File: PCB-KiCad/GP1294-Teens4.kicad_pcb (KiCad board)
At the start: 2 copper layers, 178.3 x 100.1 mm, 51 parts, among them IC1 74132D, IC2 XL6009, IC3 ZXBM5210, SW1 SW_DPDT_x2, SW2 SW_DPDT_x2, SW3 SW_DPDT_x2, SW4 SW_DPDT_x2, SW5 SW_DPDT_x2, U3 R-78B5.0-2.0, U5 ATtiny84A-P, U6 74HC165, U7 74HC165, U8 CS8421

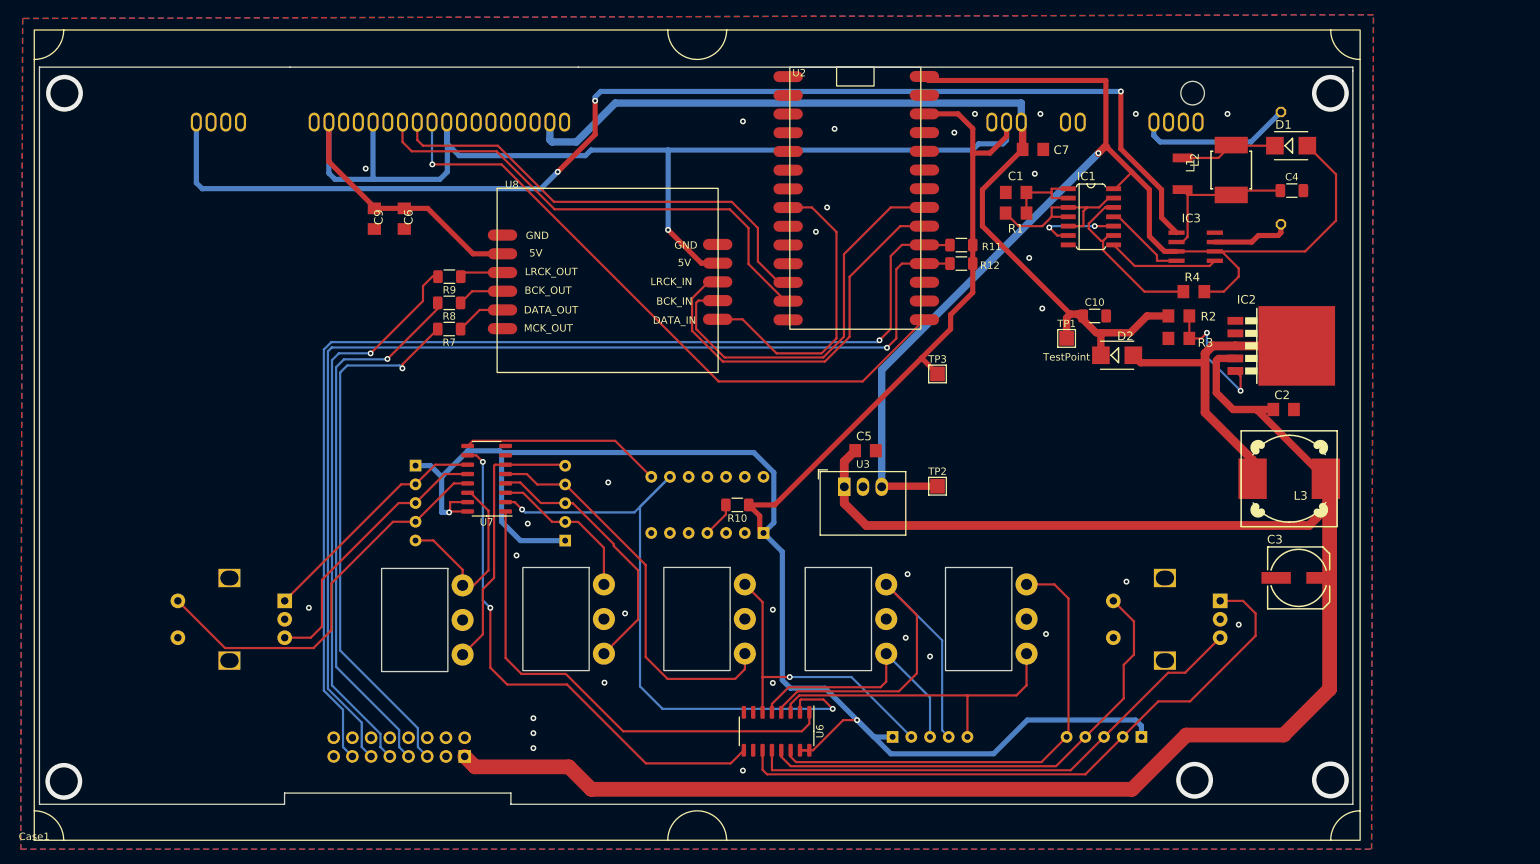
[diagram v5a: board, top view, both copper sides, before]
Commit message: Added OLED 5.5" option
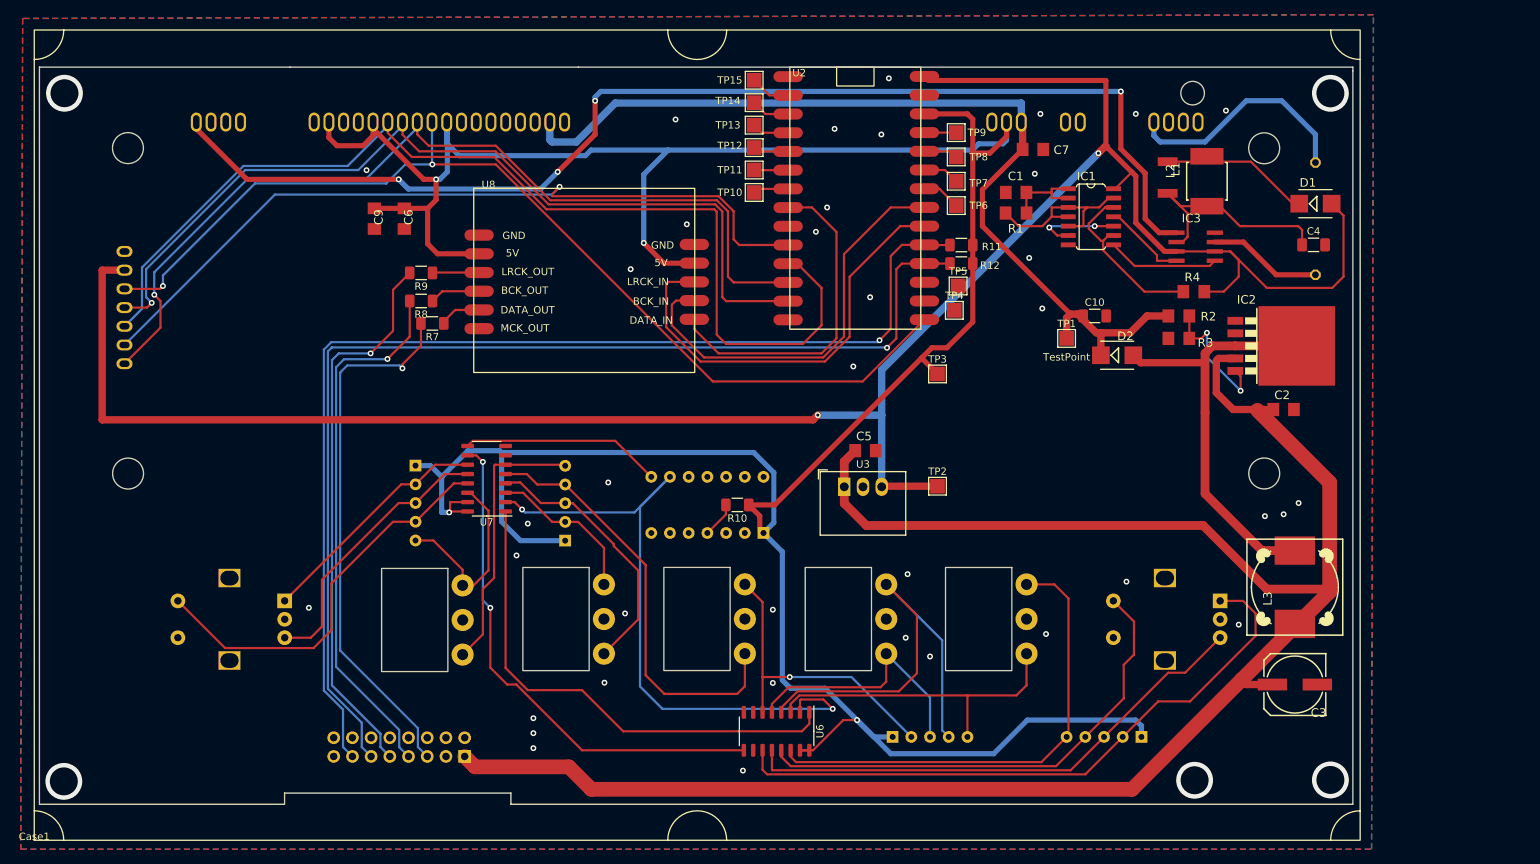
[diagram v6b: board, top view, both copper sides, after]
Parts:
- added TP10: TestPoint, TestPoint:TestPoint_Pad_2.0x2.0mm, F.Cu at (157.7, 67.1)
- added TP11: TestPoint, TestPoint:TestPoint_Pad_2.0x2.0mm, F.Cu at (157.7, 64.0)
- added TP12: TestPoint, TestPoint:TestPoint_Pad_2.0x2.0mm, F.Cu at (157.7, 61.0)
- added TP13: TestPoint, TestPoint:TestPoint_Pad_2.0x2.0mm, F.Cu at (157.7, 57.9)
- added TP14: TestPoint, TestPoint:TestPoint_Pad_2.0x2.0mm, F.Cu at (157.7, 54.9)
- added TP15: TestPoint, TestPoint:TestPoint_Pad_2.0x2.0mm, F.Cu at (157.7, 51.8)
- added TP4: TestPoint, TestPoint:TestPoint_Pad_2.0x2.0mm, F.Cu at (184.9, 83.1)
- added TP5: TestPoint, TestPoint:TestPoint_Pad_2.0x2.0mm, F.Cu at (185.4, 79.8)
- added TP6: TestPoint, TestPoint:TestPoint_Pad_2.0x2.0mm, F.Cu at (185.2, 68.8)
- added TP7: TestPoint, TestPoint:TestPoint_Pad_2.0x2.0mm, F.Cu at (185.2, 65.5)
- added TP8: TestPoint, TestPoint:TestPoint_Pad_2.0x2.0mm, F.Cu at (185.2, 62.2)
- added TP9: TestPoint, TestPoint:TestPoint_Pad_2.0x2.0mm, F.Cu at (185.2, 58.9)
- added U9: ~, VFDs-Library:OLED5.5, B.Cu at (229.3, 58.0)
- moved L3 14.8 mm to (231.1, 120.7), turned to 90 degrees
- moved C3 14.5 mm to (231.1, 133.9), turned to 180 degrees
- moved D1 8.54 mm to (233.9, 68.6)
- moved R5 8.31 mm to (233.9, 70.6)
- moved C4 7.93 mm to (233.7, 74.2)
- moved R9 3.87 mm to (112.5, 78.0)
- moved R8 3.82 mm to (112.5, 81.8)
- moved L2 3.64 mm to (219.2, 65.5)
- moved U8 3.17 mm to (134.4, 79.2)
- moved R7 2.41 mm to (114.0, 84.8)
- moved L1 2.09 mm to (213.9, 65.0)
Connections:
- net Net-(U1-CLK) renamed /SCLK
- net Net-(U1-CS) renamed /DISP_CS
- net Net-(U1-DIO) renamed /MOSI
- U1 pad 10: unconnected-(U1-RESET-Pad10) -> /DISP_RESET
- U2 pad 10: unconnected-(U2-8-Pad10) -> /DISP_DC
- U2 pad 11: unconnected-(U2-9-Pad11) -> /DISP_RESET
- U2 pad 16: unconnected-(U2-A0-Pad16) -> Net-(U2-A0)
- U2 pad 17: unconnected-(U2-A1-Pad17) -> Net-(U2-A1)
- U2 pad 2: unconnected-(U2-0-Pad2) -> Net-(U2-0)
- U2 pad 22: unconnected-(U2-A6-Pad22) -> Net-(U2-A6)
- U2 pad 23: unconnected-(U2-A7-Pad23) -> Net-(U2-A7)
- U2 pad 24: unconnected-(U2-A8-Pad24) -> Net-(U2-A8)
- U2 pad 25: unconnected-(U2-A9-Pad25) -> Net-(U2-A9)
- U2 pad 3: unconnected-(U2-1-Pad3) -> Net-(U2-1)
- U2 pad 4: unconnected-(U2-2-Pad4) -> Net-(U2-2)
- U2 pad 5: unconnected-(U2-3-Pad5) -> Net-(U2-3)
- U2 pad 6: unconnected-(U2-4-Pad6) -> Net-(U2-4)
- U2 pad 7: unconnected-(U2-5-Pad7) -> Net-(U2-5)
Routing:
- net /DISP_RESET: track 0.00 -> 144.8 mm
- net +5V: track 169.0 -> 297.8 mm, vias 1 -> 2
- net /DISP_DC: track 0.00 -> 106.7 mm, vias 0 -> 1
- net /DISP_CS: track 63.4 -> 124.9 mm, vias 0 -> 1
- net /MOSI: track 66.9 -> 122.5 mm, vias 0 -> 1
- net /SCLK: track 88.2 -> 137.9 mm, vias 1 -> 2
- net /Power/SW: track 49.5 -> 64.2 mm
- net +3.3V: track 449.2 -> 437.0 mm, vias 3 -> 4
- net F2: track 21.1 -> 32.2 mm
- net Net-(IC3-VM): track 22.6 -> 31.2 mm
- net Net-(D1-PadC): track 13.3 -> 20.2 mm
- net Net-(U2-0): track 0.00 -> 5.46 mm
- net Net-(U2-A6): track 0.00 -> 5.26 mm
- net Net-(U2-1): track 0.00 -> 5.25 mm
- net Net-(U2-2): track 0.00 -> 5.04 mm
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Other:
- outline, holes or cut-outs redrawn

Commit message: Upgraded Power circuit.
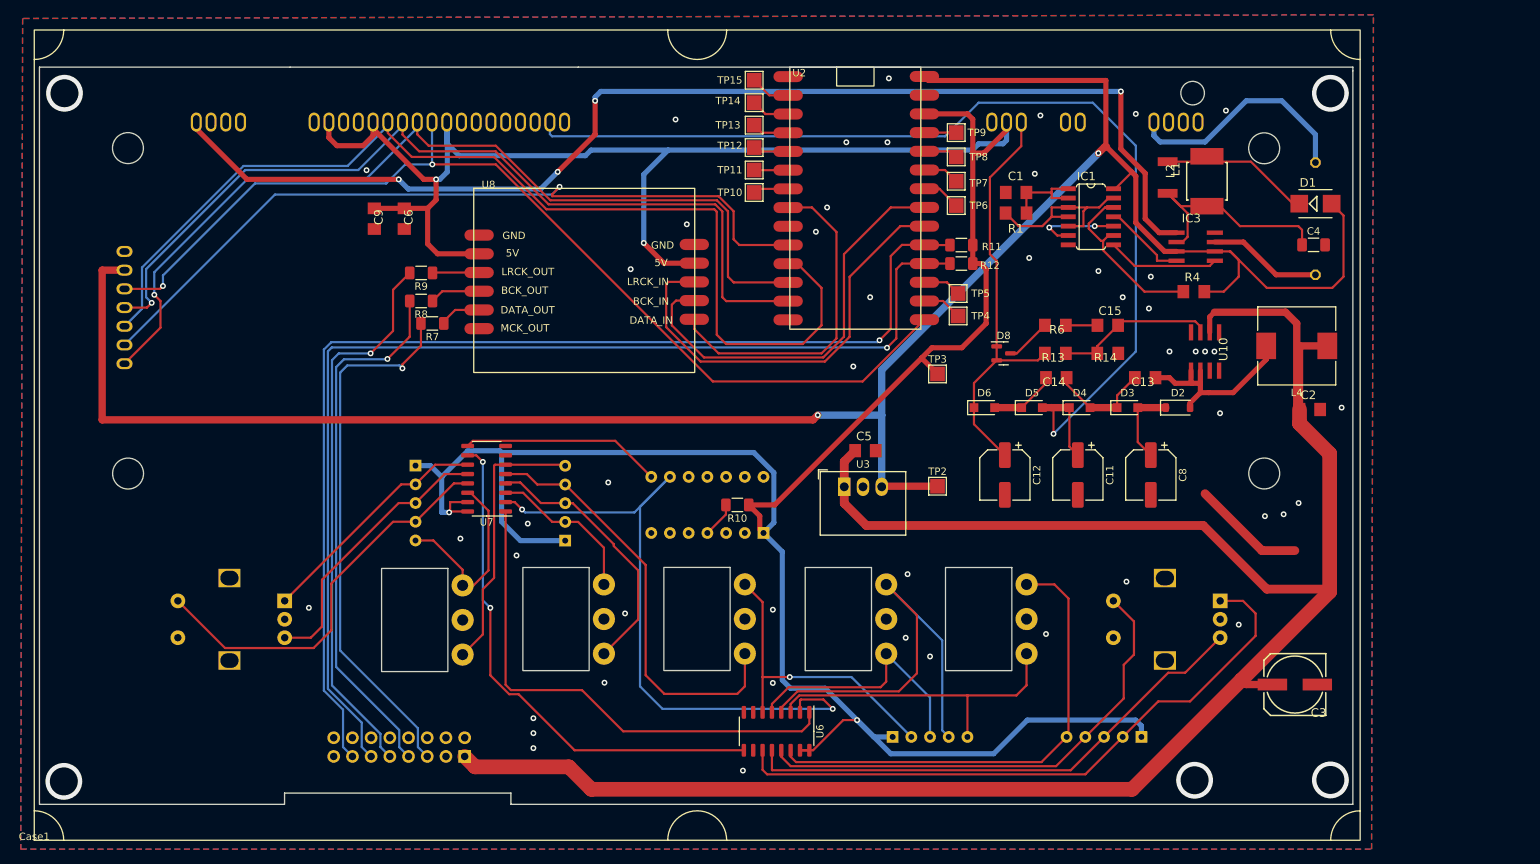
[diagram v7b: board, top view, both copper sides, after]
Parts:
- removed C10: 1u, Capacitor_SMD:C_1206_3216Metric_Pad1.33x1.80mm_HandSolder
- removed C7: 100n, VFD-Power:C1206
- removed IC2: XL6009, VFD-Power:TO263-5
- removed L3: 33uH, VFD-Power:DR125
- removed R2: 1.5k, VFD-Power:R1206
- removed R3: 39, VFD-Power:R1206
- removed TP1: TestPoint, TestPoint:TestPoint_Pad_2.0x2.0mm
- added C11: 4.7u/100v, Capacitor_SMD:CP_Elec_6.3x5.8, F.Cu at (201.7, 105.4)
- added C12: 4.7u/100v, Capacitor_SMD:CP_Elec_6.3x5.8, F.Cu at (191.8, 105.4)
- added C13: 1u/100v, VFD-Power:C1206, F.Cu at (210.8, 92.2)
- added C14: 1u/100v, VFD-Power:C1206, F.Cu at (198.8, 92.2)
- added C15: 1u/100v, VFD-Power:C1206, F.Cu at (205.7, 85.1)
- added C8: 47u/35v, Capacitor_SMD:CP_Elec_6.3x5.8, F.Cu at (211.6, 105.4)
- added D3: 1N4448W, Diode_SMD:Nexperia_CFP3_SOD-123W, F.Cu at (208.4, 96.3)
- added D4: 1N4448W, Diode_SMD:Nexperia_CFP3_SOD-123W, F.Cu at (201.9, 96.3)
- added D5: 1N4448W, Diode_SMD:Nexperia_CFP3_SOD-123W, F.Cu at (195.5, 96.3)
- added D6: 1N4448W, Diode_SMD:Nexperia_CFP3_SOD-123W, F.Cu at (189.0, 96.3)
- added D8: BAT54S, Package_TO_SOT_SMD:SOT-23, F.Cu at (191.6, 88.9)
- added L4: 22uH, Inductor_SMD:L_10.4x10.4_H4.8, F.Cu at (231.4, 87.9)
- added R13: 91k, VFD-Power:R1206, F.Cu at (198.6, 88.9)
- added R14: 2k, VFD-Power:R1206, F.Cu at (205.7, 88.9)
- added R6: 1k, VFD-Power:R1206, F.Cu at (198.6, 85.1)
- added U10: ~, VFD-Power:SO8, F.Cu at (218.9, 88.6)
- D2: value SW-SMB -> 1N4448W; footprint VFD-Power:SMB -> Diode_SMD:D_SOD-123
- moved D2 10.9 mm to (215.3, 96.3)
- moved C2 3.56 mm to (233.2, 96.5)
- moved TP5 1.02 mm to (185.4, 80.8)
- moved TP4 0.92 mm to (185.4, 83.8)
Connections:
- U1 pad 21: VPP -> VHG
- U1 pad 25: VPP -> VHP
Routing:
- net VHG: track 0.00 -> 143.6 mm, vias 0 -> 1
- net VPP: track 126.5 -> 0.00 mm
- net /Power/SW: track 64.2 -> 0.00 mm
- net VHP: track 0.00 -> 57.3 mm
- net Net-(D2-A): track 0.00 -> 26.4 mm
- net Net-(U10-FB): track 0.00 -> 21.7 mm
- net +24V: track 257.9 -> 278.8 mm
- net Net-(IC2-FB): track 18.5 -> 0.00 mm, vias 2 -> 0
- net (no net): track 0.00 -> 15.4 mm, vias 0 -> 1
- net Net-(D3-K): track 0.00 -> 14.1 mm
- net Net-(D2-K): track 0.00 -> 11.0 mm
- net Net-(D5-K): track 0.00 -> 9.11 mm
- net Net-(D8-COM): track 0.00 -> 6.25 mm
- net Net-(U2-A0): track 0.00 -> 5.41 mm
- net Net-(U2-A1): track 0.00 -> 5.20 mm
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
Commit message: Added Debounce Caps and stuff.
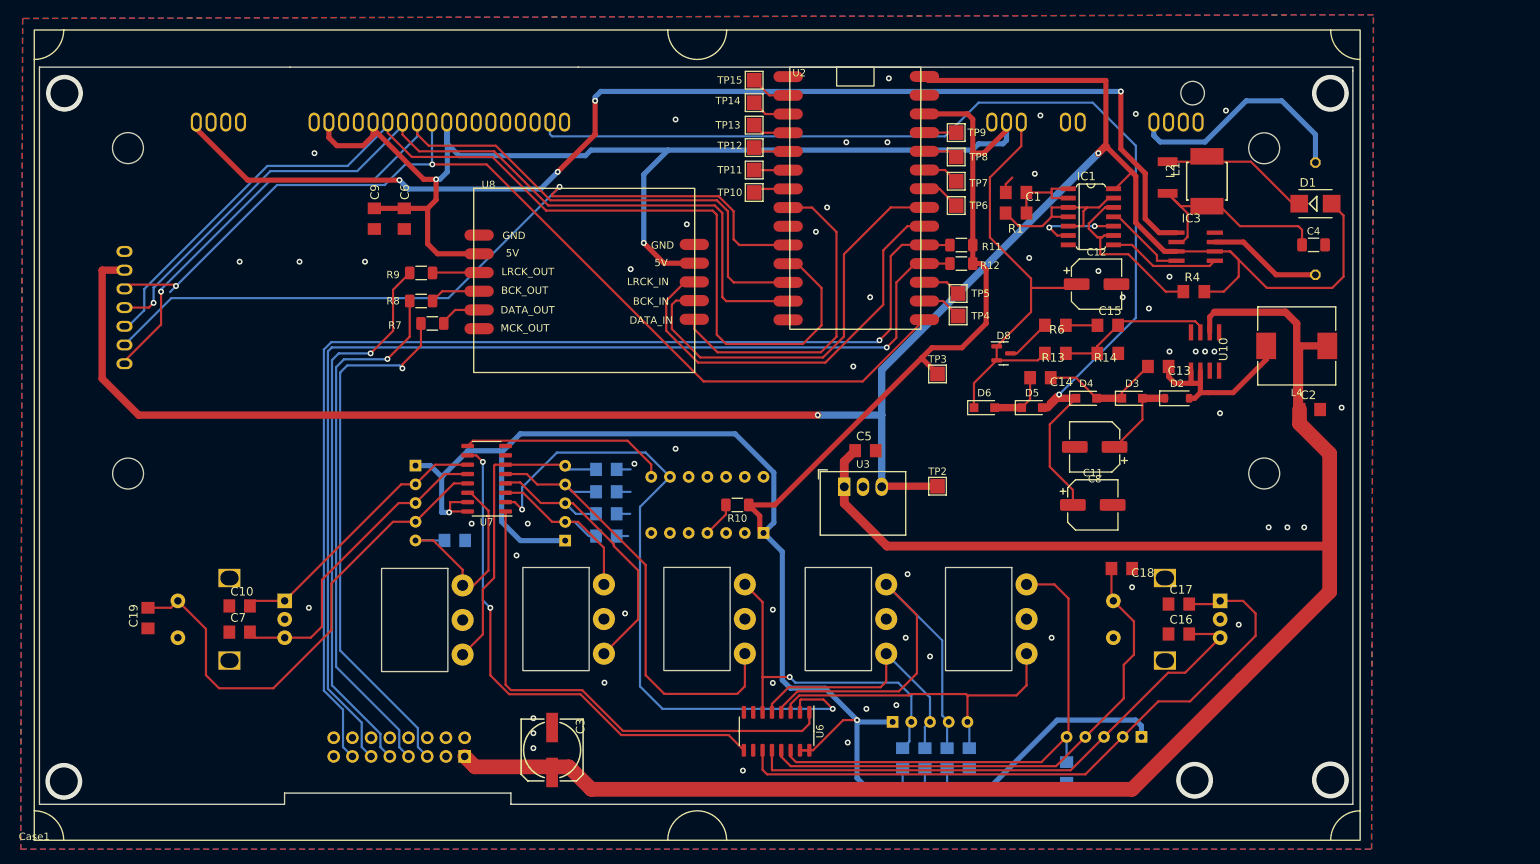
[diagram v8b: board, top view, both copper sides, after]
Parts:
- added C10: 10n, VFD-Power:C1206, F.Cu at (87.9, 123.2)
- added C16: 10n, VFD-Power:C1206, F.Cu at (215.4, 127.0)
- added C17: 10n, VFD-Power:C1206, F.Cu at (215.4, 122.9)
- added C18: 10n, VFD-Power:C1206, F.Cu at (207.6, 118.1)
- added C19: 10n, VFD-Power:C1206, F.Cu at (75.4, 124.8)
- added C20: 10n, VFD-Power:C1206, B.Cu at (200.2, 145.8)
- added C21: 10n, VFD-Power:C1206, B.Cu at (186.9, 143.9)
- added C22: 10n, VFD-Power:C1206, B.Cu at (183.9, 143.9)
- added C23: 10n, VFD-Power:C1206, B.Cu at (180.9, 143.9)
- added C24: 10n, VFD-Power:C1206, B.Cu at (177.9, 143.9)
- added C25: 10n, VFD-Power:C1206, B.Cu at (137.7, 107.7)
- added C26: 10n, VFD-Power:C1206, B.Cu at (137.7, 113.7)
- added C27: 10n, VFD-Power:C1206, B.Cu at (137.7, 110.7)
- added C28: 10n, VFD-Power:C1206, B.Cu at (117.1, 114.3)
- added C29: 10n, VFD-Power:C1206, B.Cu at (137.7, 104.6)
- added C7: 10n, VFD-Power:C1206, F.Cu at (87.9, 126.7)
- moved C3 101.2 mm to (130.3, 142.7), turned to -90 degrees
- moved C12 28.7 mm to (204.2, 79.5), turned to 0 degrees
- moved C8 8.52 mm to (204.0, 101.6), turned to 180 degrees
- moved C11 4.54 mm to (203.7, 109.5), turned to 0 degrees
- moved C13 2.34 mm to (212.6, 90.7)
- moved C14 2.16 mm to (196.6, 92.2)
- moved RN2 2.03 mm to (176.5, 138.9)
- moved D4 1.55 mm to (202.8, 95.0)
- moved D3 1.42 mm to (209.0, 95.0)
- moved D2 1.28 mm to (215.1, 95.0)
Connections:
- net Net-(RN1-R4) renamed /inputs/S1
- net Net-(RN2-R1) renamed /inputs/S5
- net Net-(RN2-R2) renamed /inputs/S4
- net Net-(RN2-R3) renamed /inputs/S3
- net Net-(RN2-R4) renamed /inputs/S2
- net Net-(RN3-R4) renamed /inputs/S9
- net Net-(RN4-R1) renamed /inputs/S7
- net Net-(RN4-R2) renamed /inputs/S8
- net Net-(RN4-R3) renamed /inputs/S6
- net Net-(RN4-R4) renamed /inputs/S10
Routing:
- net (no net): track 15.4 -> 0.00 mm, vias 1 -> 0
- net GND: track 0.00 -> 15.2 mm, vias 52 -> 60
- net /inputs/enc2c: track 55.0 -> 67.6 mm
- net +3.3V: track 439.9 -> 450.2 mm
- net /inputs/S5: track 41.9 -> 47.2 mm
- net VHG: track 143.6 -> 148.8 mm
- net /inputs/enc2b: track 37.8 -> 42.8 mm
- net /inputs/enc2a: track 32.5 -> 37.5 mm
- net /inputs/S7: track 21.4 -> 26.4 mm
- net /inputs/S8: track 36.4 -> 41.2 mm
- net /inputs/S6: track 58.5 -> 63.1 mm
- net /inputs/enc1c: track 66.7 -> 71.2 mm
- net /inputs/enc1b: track 71.0 -> 75.4 mm
- net /inputs/S10: track 37.2 -> 41.6 mm
- net /inputs/enc1a: track 86.2 -> 90.6 mm
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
